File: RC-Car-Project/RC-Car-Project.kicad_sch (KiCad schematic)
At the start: 4 parts

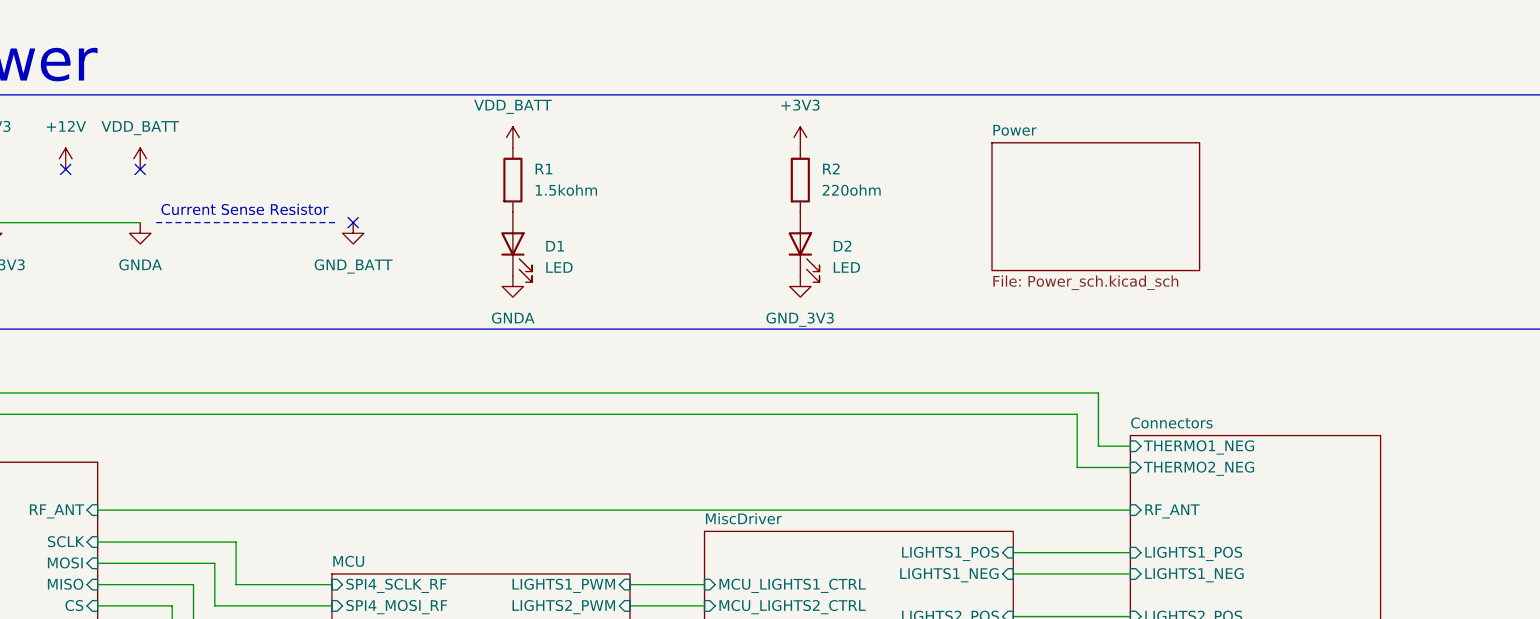
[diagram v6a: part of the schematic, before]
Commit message: Add switch
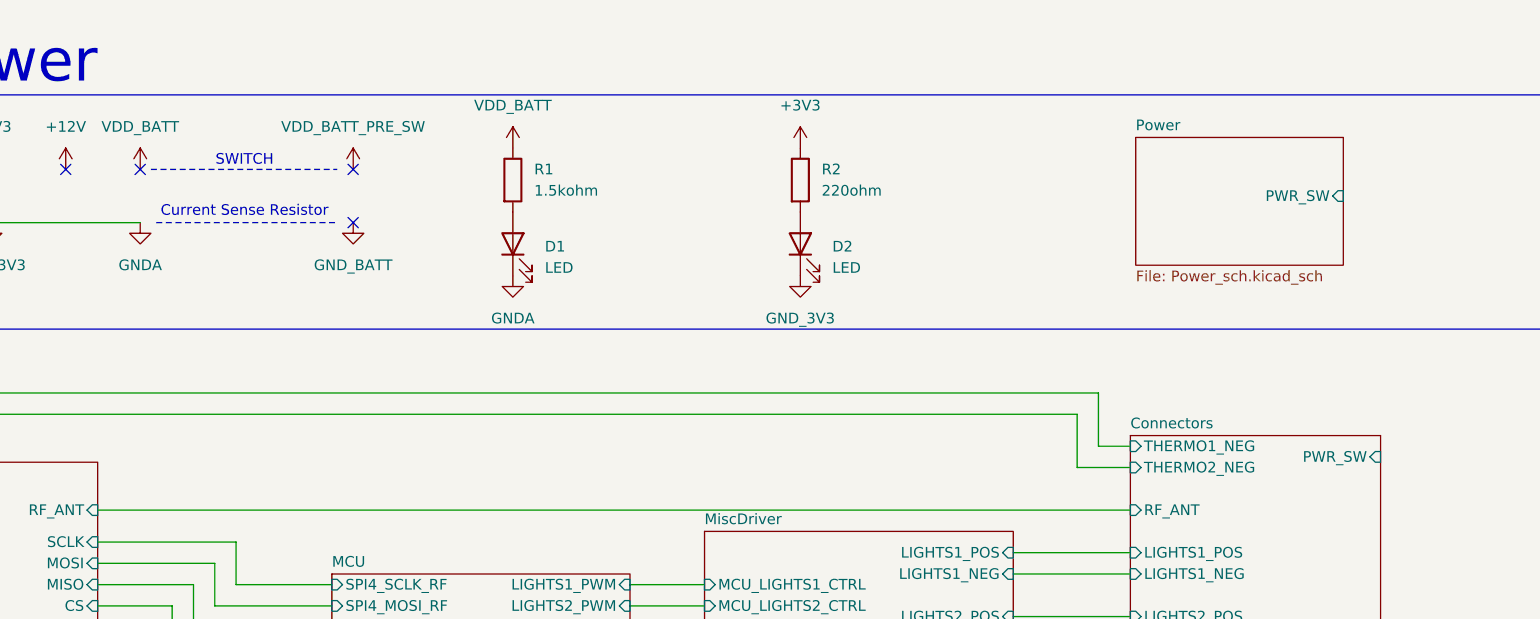
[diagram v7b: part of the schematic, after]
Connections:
- no-connect marks 5 -> 6
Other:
- sheet Connectors ports: added PWR_SW; removed none
- sheet Power ports: added PWR_SW; removed none
- note added: "SWITCH"
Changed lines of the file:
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@@
+	)
+	(no_connect
+		(at 115.57 34.29)
 	)
 	(no_connect
@@
 	(wire
 		(pts
-			(xy 208.28 67.31) (xy 204.47 67.31)
-		)
-		(stroke
-			(width 0)
-			(type default)
-		)
-	)
-	(wire
-		(pts
 			(xy 194.31 80.01) (xy 208.28 80.01)
 		)
@@
 	(wire
 		(pts
+			(xy 204.47 67.31) (xy 208.28 67.31)
+		)
+		(stroke
+			(width 0)
+			(type default)
+		)
+	)
+	(wire
+		(pts
 			(xy 113.03 86.36) (xy 99.06 86.36)
 		)
@@
 			(width 0)
 			(type default)
+		)
+	)
+	(polyline
+		(pts
+			(xy 91.44 34.29) (xy 113.665 34.29)
+		)
+		(stroke
+			(width 0)
+			(type dash_dot)
+			(color 255 5 28 1)
 		)
 	)
@@
 		(fill
 			(type none)
+		)
+	)
+	(text "SWITCH"
+		(exclude_from_sim no)
+		(at 102.616 33.274 0)
+		(effects
+			(font
+				(size 1.27 1.27)
+			)
 		)
 	)
@@
 	)
 	(symbol
+		(lib_id "power:+3V3")
+		(at 115.57 34.29 0)
+		(unit 1)
+		(exclude_from_sim no)
+		(in_bom yes)
+		(on_board yes)
+		(dnp no)
+		(fields_autoplaced yes)
+		(property "Reference" "#PWR0133"
+			(at 115.57 38.1 0)
+			(effects
+				(font
+					(size 1.27 1.27)
+				)
+				(hide yes)
+			)
+		)
+		(property "Value" "VDD_BATT_PRE_SW"
+			(at 115.57 29.21 0)
+			(effects
+				(font
+					(size 1.27 1.27)
+				)
+			)
+		)
+		(property "Footprint" ""
+			(at 115.57 34.29 0)
+			(effects
+				(font
+					(size 1.27 1.27)
+				)
+				(hide yes)
+			)
+		)
+		(property "Datasheet" ""
+			(at 115.57 34.29 0)
+			(effects
+				(font
+					(size 1.27 1.27)
+				)
+				(hide yes)
+			)
+		)
+		(property "Description" "Power symbol creates a global label with name \"+3V3\""
+			(at 115.57 34.29 0)
+			(effects
+				(font
+					(size 1.27 1.27)
+				)
+				(hide yes)
+			)
+		)
+		(pin "1"
+		)
+		(instances
+			(project "RC-Car-Project"
+				(path "/ba870fd1-751d-4755-8e1a-1ea86ca9e2f6"
+					(reference "#PWR0133")
+					(unit 1)
+				)
+			)
+		)
+	)
+	(symbol
 		(lib_id "power:GND")
 		(at 115.57 40.64 0)
@@
 			)
 		)
+		(pin "PWR_SW" input
+			(at 238.125 68.58 0)
+			(effects
+				(font
+					(size 1.27 1.27)
+				)
+				(justify right)
+			)
+		)
 		(instances
 			(project "RC-Car-Project"
@@
 	)
 	(sheet
-		(at 191.77 31.115)
+		(at 208.915 30.48)
 		(size 24.765 15.24)
 		(fields_autoplaced yes)
@@
 		)
 		(property "Sheetname" "Power"
-			(at 191.77 30.4034 0)
+			(at 208.915 29.7684 0)
 			(effects
 				(font
@@
 		)
 		(property "Sheetfile" "Power_sch.kicad_sch"
-			(at 191.77 46.9396 0)
+			(at 208.915 46.3046 0)
 			(effects
 				(font
@@
 			)
 		)
+		(pin "PWR_SW" input
+			(at 233.68 37.465 0)
+			(effects
+				(font
+					(size 1.27 1.27)
+				)
+				(justify right)
+			)
+		)

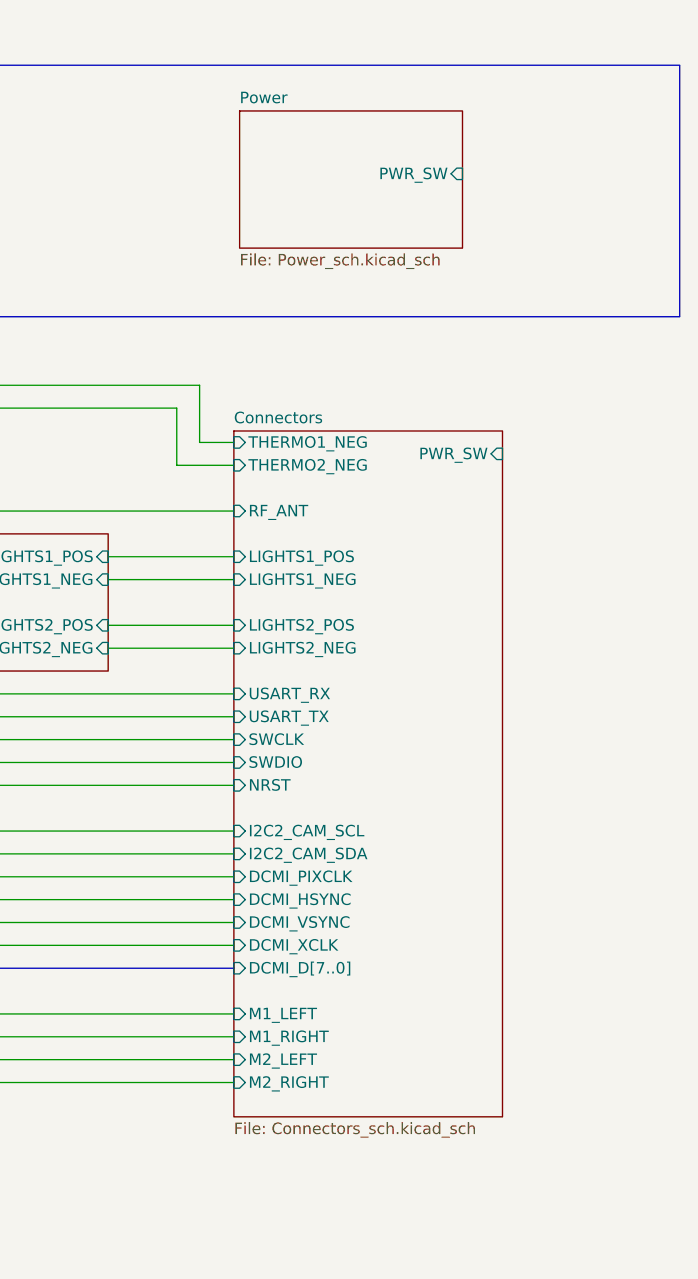
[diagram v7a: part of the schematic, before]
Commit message: Fixed Borked Connectors
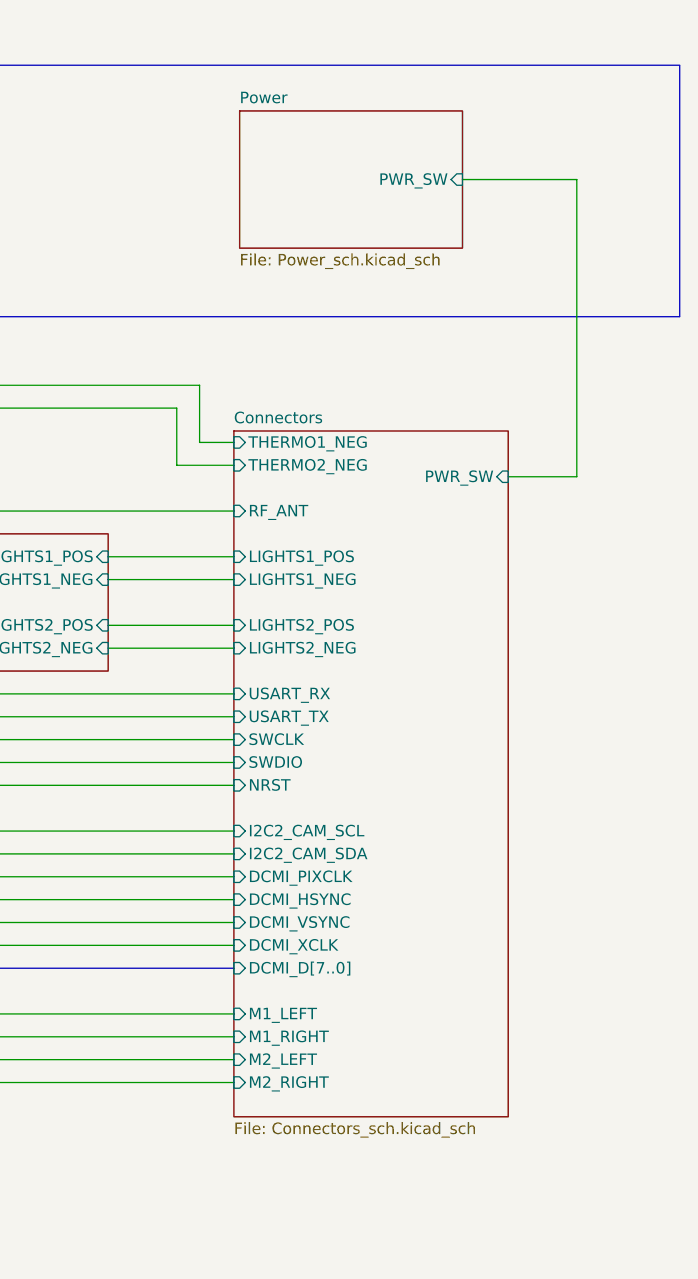
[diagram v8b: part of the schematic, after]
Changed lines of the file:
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@@
+	(wire
+		(pts
+			(xy 233.68 38.1) (xy 246.38 38.1)
+		)
+		(stroke
+			(width 0)
+			(type default)
+		)
+	)
 	(wire
 		(pts
@@
 	(wire
 		(pts
+			(xy 246.38 38.1) (xy 246.38 71.12)
+		)
+		(stroke
+			(width 0)
+			(type default)
+		)
+	)
+	(wire
+		(pts
 			(xy 148.59 115.57) (xy 208.28 115.57)
 		)
@@
 		(pts
 			(xy 161.29 135.89) (xy 208.28 135.89)
+		)
+		(stroke
+			(width 0)
+			(type default)
+		)
+	)
+	(wire
+		(pts
+			(xy 246.38 71.12) (xy 238.76 71.12)
 		)
 		(stroke
@@
 	(sheet
 		(at 208.28 66.04)
-		(size 29.845 76.2)
+		(size 30.48 76.2)
 		(fields_autoplaced yes)
 		(stroke
@@
 		)
 		(pin "PWR_SW" input
-			(at 238.125 68.58 0)
+			(at 238.76 71.12 0)
 			(effects
 				(font
@@
 		)
 		(pin "PWR_SW" input
-			(at 233.68 37.465 0)
-			(effects
-				(font
+			(at 233.68 38.1 0)
+			(effects
+				(font
